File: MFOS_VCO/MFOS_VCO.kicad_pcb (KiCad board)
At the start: 4 copper layers, 100 x 70 mm, 106 parts, among them J12 Conn_01x01, J13 Conn_01x01, J14 Conn_01x01, J15 Conn_01x01, J16 Conn_01x01, J17 Conn_01x01, J18 Conn_01x01, J19 Conn_01x01, J21 Conn_01x01, J22 Conn_01x01, J23 Conn_01x01, J25 Conn_01x01, Q1 PN4391, U1 OP275, U2 TL072, U3 SSM2212, U4 TL074, U5 LM13700, U6 TL072, U7 TL071

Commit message: Laying out
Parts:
- removed J13, J14, J22: Conn_01x01, Connector_Pin:Pin_D1.0mm_L10.0mm_LooseFit
- removed R2, R3, R39: 100k, Resistor_THT:R_Axial_DIN0207_L6.3mm_D2.5mm_P7.62mm_Horizontal
- added J1: Conn_02x05_Odd_Even, Connector_IDC:IDC-Header_2x05_P2.54mm_Vertical, F.Cu at (107.0, 99.5)
- added J24: Conn_01x03, Connector_PinHeader_2.54mm:PinHeader_1x03_P2.54mm_Vertical, F.Cu at (121.7, 68.1)
- added J26: Conn_01x03, Connector_PinHeader_2.54mm:PinHeader_1x03_P2.54mm_Vertical, F.Cu at (121.9, 77.0)
- added J27: Conn_01x03, Connector_PinHeader_2.54mm:PinHeader_1x03_P2.54mm_Vertical, F.Cu at (78.2, 85.9)
- C10, C7: footprint Capacitor_THT:C_Radial_D4.0mm_H5.0mm_P1.50mm -> Capacitor_THT:CP_Radial_D4.0mm_P1.50mm
- J12: value Conn_01x01 -> Conn_01x04; footprint Connector_Pin:Pin_D1.0mm_L10.0mm_LooseFit -> Connector_PinHeader_2.54mm:PinHeader_1x04_P2.54mm_Vertical
- J15: footprint Connector_Pin:Pin_D1.0mm_L10.0mm_LooseFit -> Connector_Pin:Pin_D0.9mm_L10.0mm_W2.4mm_FlatFork
- R11, R16, R5, R59, R60, R64, R7: footprint Resistor_THT:R_Axial_DIN0207_L6.3mm_D2.5mm_P7.62mm_Horizontal -> Potentiometer_THT:Potentiometer_Bourns_3339P_Vertical
- moved U5 296.5 mm to (210.5, 85.9)
- moved R24 224.9 mm to (118.9, 99.8), turned to 90 degrees
- moved C3 224.9 mm to (121.9, 116.1)
- moved D1 219.5 mm to (125.2, 92.5), turned to -90 degrees
- moved U1 216.8 mm to (111.0, 109.2)
- moved R71 215.4 mm to (132.3, 76.7), turned to 180 degrees
- moved C19 215.2 mm to (121.7, 87.6), turned to 90 degrees
- moved R17 211.5 mm to (115.6, 103.6)
- moved R9 211.2 mm to (128.0, 92.5), turned to -90 degrees
- moved R11 210.8 mm to (127.5, 110.2), turned to 90 degrees
- moved R56 203.6 mm to (132.3, 67.6), turned to 180 degrees
- moved R18 199.3 mm to (117.1, 70.4), turned to 180 degrees
- moved R65 196.6 mm to (124.7, 82.8)
- moved R57 194.5 mm to (124.7, 73.7)
- moved U2 192.8 mm to (83.6, 106.2)
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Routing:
- net +12V: track 0.00 -> 313.1 mm, vias 0 -> 5
- net -12V: track 0.00 -> 287.1 mm, vias 0 -> 1
- net Net-(C19-Pad1): track 0.00 -> 84.1 mm, vias 0 -> 2
- net Net-(C3-Pad1): track 0.00 -> 42.1 mm, vias 0 -> 1
- net Net-(C19-Pad2): track 0.00 -> 41.9 mm, vias 0 -> 1
- net Net-(D1-Pad2): track 0.00 -> 25.5 mm, vias 0 -> 1
- net Net-(C3-Pad2): track 0.00 -> 18.0 mm
- net Net-(R17-Pad1): track 0.00 -> 15.3 mm, vias 0 -> 1
- net Net-(R11-Pad1): track 0.00 -> 14.0 mm
- net Net-(R16-Pad3): track 0.00 -> 9.99 mm
- net CV1: track 0.00 -> 3.36 mm
- net /R3P1: track 0.00 -> 3.26 mm
- net CV4: track 0.00 -> 3.26 mm
- net CV2: track 0.00 -> 3.26 mm
- net /R3P3: track 0.00 -> 3.25 mm
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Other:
- rule pad_to_mask_clearance: 3.15 -> 0.0889
- board text added: "+12V"
- board text added: "-12V"
- board text added: "GND"

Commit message: Laid out last part of sheet 1
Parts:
- removed J15: Conn_01x01, Connector_Pin:Pin_D0.9mm_L10.0mm_W2.4mm_FlatFork
- removed J17: Conn_01x01, Connector_Pin:Pin_D1.0mm_L10.0mm_LooseFit
- added J13: Conn_01x02, Connector_PinHeader_2.54mm:PinHeader_1x02_P2.54mm_Vertical, F.Cu at (113.8, 120.1)
- moved C6 254.5 mm to (146.4, 97.8), turned to 180 degrees
- moved C17 244.9 mm to (142.5, 113.5), turned to 90 degrees
- moved D8 239.7 mm to (131.6, 118.6)
- moved R50 232.3 mm to (131.6, 121.4)
- moved R70 228.2 mm to (131.6, 124.7)
- moved R69 226.8 mm to (145.3, 111.3), turned to 90 degrees
- moved R42 219.4 mm to (131.8, 114.3)
- moved R46 211.6 mm to (142.5, 92.5), turned to 180 degrees
- moved C18 209.3 mm to (142.5, 108.9), turned to 90 degrees
- moved C8 204.8 mm to (132.1, 90.2), turned to -90 degrees
- moved R66 203.4 mm to (120.4, 124.7)
- moved R34 194.0 mm to (120.4, 121.7)
- moved Q1 192.6 mm to (128.3, 118.6), turned to 90 degrees
- moved R47 187.9 mm to (142.5, 89.4), turned to 180 degrees
- moved R31 183.6 mm to (114.6, 123.7), turned to 180 degrees
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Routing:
- net LIN: track 2.90 -> 9.84 mm
- net SYNC: track 0.00 -> 2.96 mm
- net Net-(C5-Pad2): track 0.00 -> 2.73 mm
- net GND: track 0.00 -> 2.39 mm, vias 0 -> 1
- net -12V: track 287.1 -> 288.2 mm
- net Net-(D1-Pad2): track 25.5 -> 25.2 mm, vias 1 -> 3

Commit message: All done
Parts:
- removed J16, J18, J19, J21, J23, J25: Conn_01x01, Connector_Pin:Pin_D1.0mm_L10.0mm_LooseFit
- added G***: LOGO, LOGO, F.Cu at (194.6, 119.9)
- added J14: Conn_01x02, Connector_PinHeader_2.54mm:PinHeader_1x02_P2.54mm_Vertical, F.Cu at (194.6, 73.4)
- added J15: Conn_01x04, Connector_PinHeader_2.54mm:PinHeader_1x04_P2.54mm_Vertical, F.Cu at (191.0, 105.2)
- added kibuzzard-65B0951C: G***, kibuzzard-65B0951C, F.Cu at (110.2, 62.2)
- added kibuzzard-65B09543: G***, kibuzzard-65B09543, F.Cu at (190.5, 119.6)
- C12: footprint Capacitor_THT:CP_Radial_D8.0mm_P3.50mm -> Capacitor_THT:CP_Radial_D5.0mm_P2.00mm
- C13: footprint Capacitor_THT:CP_Radial_D8.0mm_P3.50mm -> Capacitor_THT:CP_Radial_D5.0mm_P2.50mm
- moved R36 292.6 mm to (188.0, 99.3)
- moved U7 281.1 mm to (177.0, 86.6)
- moved R64 280.8 mm to (176.3, 111.3)
- moved R67 279.5 mm to (173.7, 93.2), turned to 180 degrees
- moved R60 278.4 mm to (184.6, 111.2)
- moved D4 278.3 mm to (171.4, 75.2), turned to 180 degrees
- moved R40 271.0 mm to (166.1, 90.2)
- moved R49 269.9 mm to (186.7, 124.2), turned to 90 degrees
- moved R48 269.1 mm to (163.8, 116.6), turned to -90 degrees
- moved R41 267.8 mm to (195.6, 96.0), turned to 180 degrees
- moved R53 264.3 mm to (180.6, 124.2), turned to 90 degrees
- moved U4 262.9 mm to (153.4, 87.1)
- moved R29 261.6 mm to (167.9, 100.8)
- moved R35 261.1 mm to (177.0, 83.3)
- moved U6 259.9 mm to (177.0, 68.8)
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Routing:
- net +12V: track 313.1 -> 481.0 mm, vias 5 -> 11
- net -12V: track 288.2 -> 395.1 mm, vias 1 -> 2
- net Net-(C6-Pad1): track 0.00 -> 67.5 mm, vias 0 -> 4
- net Net-(D3-Pad2): track 0.00 -> 62.5 mm
- net TRI: track 0.00 -> 61.3 mm, vias 0 -> 3
- net Net-(R14-Pad2): track 0.00 -> 47.2 mm, vias 0 -> 3
- net PWM: track 0.00 -> 46.8 mm, vias 0 -> 1
- net RMP: track 0.00 -> 45.3 mm
- net Net-(R34-Pad2): track 0.00 -> 44.4 mm, vias 0 -> 3
- net Net-(C12-Pad2): track 0.00 -> 41.9 mm, vias 0 -> 4
- net RAW: track 0.00 -> 40.5 mm, vias 0 -> 2
- net Net-(C2-Pad1): track 0.00 -> 40.0 mm, vias 0 -> 1
- net Net-(C14-Pad1): track 0.00 -> 33.7 mm, vias 0 -> 3
- net Net-(R13-Pad2): track 0.00 -> 32.6 mm, vias 0 -> 1
- net Net-(R45-Pad2): track 0.00 -> 31.9 mm, vias 0 -> 3
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- added copper zone on F.Cu, net (none)

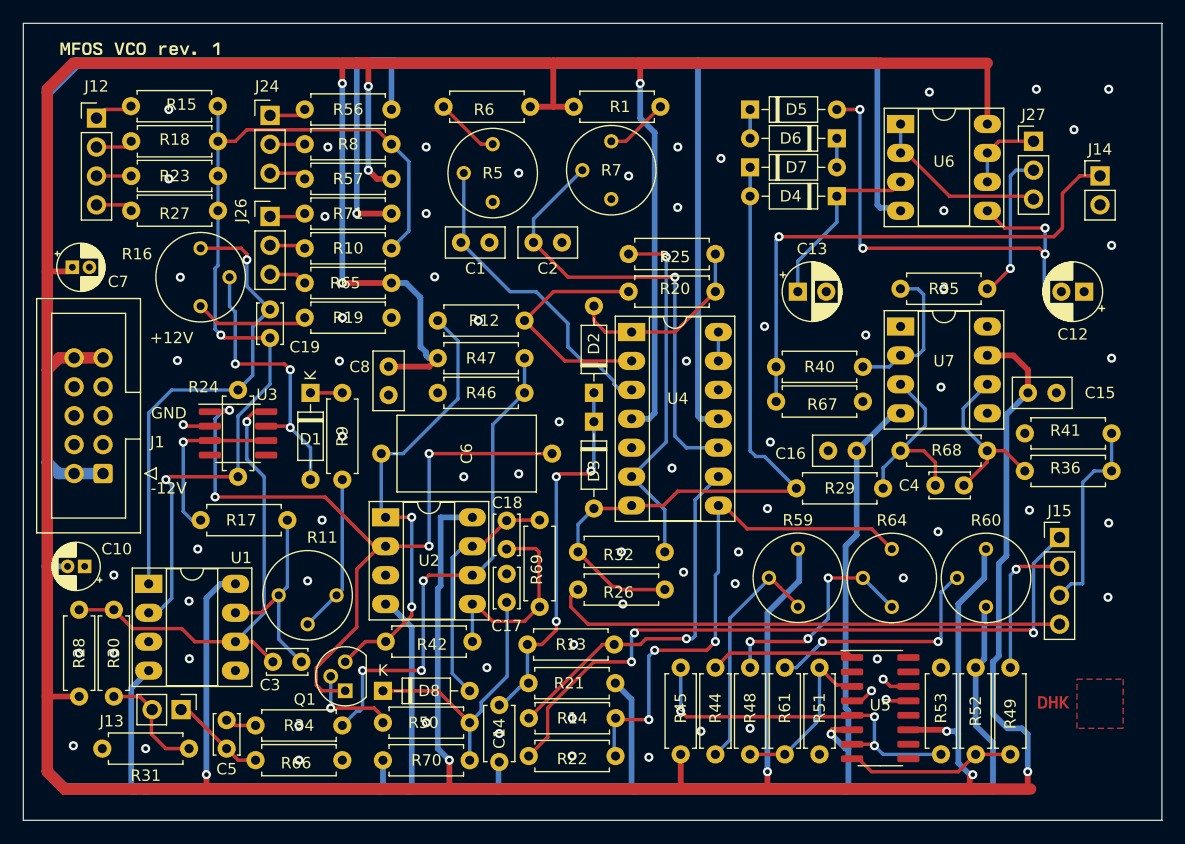
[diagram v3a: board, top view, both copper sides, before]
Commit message: Fixed PN4391 bug. Made some layout changes. Fitted molex connectors instead of pin connectors
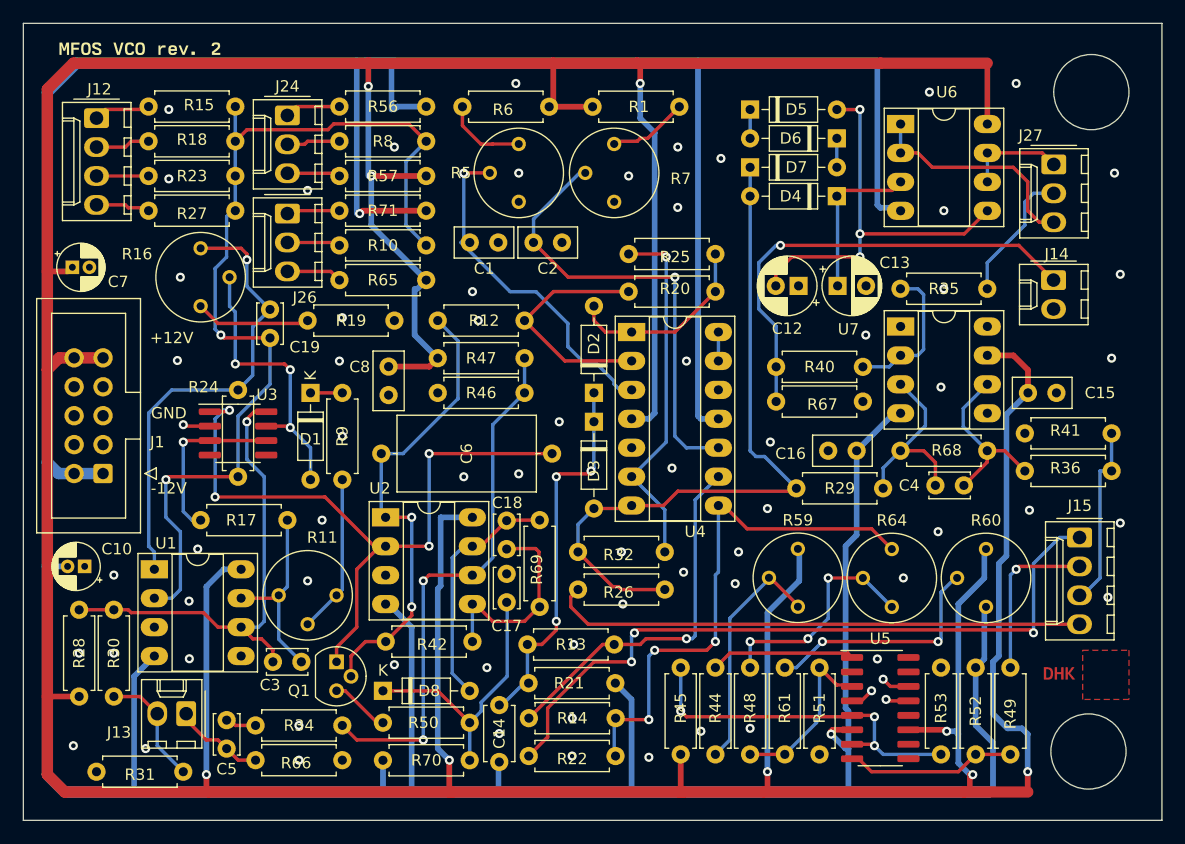
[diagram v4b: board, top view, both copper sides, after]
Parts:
- removed kibuzzard-65B0951C: G***, kibuzzard-65B0951C
- added kibuzzard-660EFCED: G***, kibuzzard-660EFCED, F.Cu at (110.2, 62.2)
- J12, J15: footprint Connector_PinHeader_2.54mm:PinHeader_1x04_P2.54mm_Vertical -> Connector_Molex:Molex_KK-254_AE-6410-04A_1x04_P2.54mm_Vertical
- J13, J14: footprint Connector_PinHeader_2.54mm:PinHeader_1x02_P2.54mm_Vertical -> Connector_Molex:Molex_KK-254_AE-6410-02A_1x02_P2.54mm_Vertical
- J24, J26, J27: footprint Connector_PinHeader_2.54mm:PinHeader_1x03_P2.54mm_Vertical -> Connector_Molex:Molex_KK-254_AE-6410-03A_1x03_P2.54mm_Vertical
- moved C12 25.1 mm to (168.1, 83.1)
- moved J14 10.0 mm to (190.5, 82.5), turned to -90 degrees
- moved C13 3.53 mm to (171.5, 83.1)
- moved R10 3.06 mm to (127.8, 79.5)
- moved R65 3.06 mm to (127.8, 82.5)
- moved R71 3.06 mm to (135.4, 76.5)
- moved R56 3.06 mm to (135.4, 67.3)
- moved R57 3.06 mm to (127.8, 73.4)
- moved R8 3.06 mm to (127.8, 70.4)
- moved J27 2.70 mm to (190.5, 72.4), turned to -90 degrees
- moved Q1 2.65 mm to (127.5, 116.1), turned to -90 degrees
- moved G*** 2.59 mm to (195.1, 117.3)
- moved kibuzzard-65B09543 2.59 mm to (191.0, 117.1)
- moved R5 2.29 mm to (143.5, 75.7)
- moved R31 2.09 mm to (114.0, 125.7)
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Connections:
- Q1 pad 2: Net-(Q1-Pad2) -> RAW
- Q1 pad 3: RAW -> Net-(Q1-Pad3)
- R50 pad 1: Net-(Q1-Pad2) -> Net-(Q1-Pad3)
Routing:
- net +12V: track 481.0 -> 470.9 mm, vias 11 -> 9
- net Net-(Q1-Pad2): track 8.20 -> 0.00 mm, vias 1 -> 0
- net -12V: track 395.1 -> 402.2 mm
- net PWM: track 46.8 -> 40.6 mm
- net Net-(C12-Pad2): track 41.9 -> 36.1 mm, vias 4 -> 3
- net Net-(C6-Pad1): track 67.5 -> 62.0 mm
- net Net-(Q1-Pad3): track 0.00 -> 5.24 mm
- net /Sheet 2/R39P3: track 15.9 -> 20.0 mm
- net Net-(R34-Pad2): track 44.4 -> 47.2 mm, vias 3 -> 2
- net Net-(C19-Pad1): track 84.1 -> 86.7 mm
- net Net-(C13-Pad1): track 16.2 -> 13.8 mm
- net Net-(C1-Pad1): track 27.9 -> 30.2 mm, vias 0 -> 1
- net /R3P3: track 3.25 -> 5.11 mm
- net /R2P3: track 3.10 -> 4.89 mm
- net /Sheet 2/R39P1: track 7.02 -> 8.79 mm
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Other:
- outline, holes or cut-outs redrawn
- rule pad_to_mask_clearance: 0.0889 -> 0

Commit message: Some bugfixes
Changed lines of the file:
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@@
     (pad_to_mask_clearance 0)
     (pcbplotparams
-      (layerselection 0x00010fc_ffffffff)
+      (layerselection 0x00010f0_ffffffff)
       (disableapertmacros false)
-      (usegerberextensions false)
+      (usegerberextensions true)
       (usegerberattributes true)
       (usegerberadvancedattributes true)
@@
     (fp_line (start -1.27 2.88) (end 6.35 2.88) (layer "F.Fab") (width 0.1))
     (fp_line (start 6.35 -2.92) (end -1.27 -2.92) (layer "F.Fab") (width 0.1))
-    (pad "1" thru_hole roundrect (at 0 0 270) (size 1.74 2.19) (drill 1.19) (layers *.Cu *.Mask) (roundrect_rratio 0.143678)
+    (pad "1" thru_hole roundrect (at 0 0 270) (size 1.74 2.19) (drill 1.19) (layers *.Cu *.Mask) (roundrect_rratio 0.1436781609)
       (net 55 "/Sheet 2/R39P1") (pinfunction "Pin_1") (pintype "passive"))
     (pad "2" thru_hole oval (at 2.54 0 270) (size 1.74 2.19) (drill 1.19) (layers *.Cu *.Mask)
@@
     (fp_line (start -1.27 2.88) (end 3.81 2.88) (layer "F.Fab") (width 0.1))
     (fp_line (start 3.81 -2.92) (end -1.27 -2.92) (layer "F.Fab") (width 0.1))
-    (pad "1" thru_hole roundrect (at 0 0 180) (size 1.74 2.19) (drill 1.19) (layers *.Cu *.Mask) (roundrect_rratio 0.143678)
+    (pad "1" thru_hole roundrect (at 0 0 180) (size 1.74 2.19) (drill 1.19) (layers *.Cu *.Mask) (roundrect_rratio 0.1436781609)
       (net 8 "SYNC") (pinfunction "Pin_1") (pintype "passive"))
     (pad "2" thru_hole oval (at 2.54 0 180) (size 1.74 2.19) (drill 1.19) (layers *.Cu *.Mask)
@@
     (fp_line (start -1.27 2.88) (end 6.35 2.88) (layer "F.Fab") (width 0.1))
     (fp_line (start -0.562893 0) (end -1.27 0.5) (layer "F.Fab") (width 0.1))
-    (pad "1" thru_hole roundrect (at 0 0 270) (size 1.74 2.19) (drill 1.19) (layers *.Cu *.Mask) (roundrect_rratio 0.143678)
+    (pad "1" thru_hole roundrect (at 0 0 270) (size 1.74 2.19) (drill 1.19) (layers *.Cu *.Mask) (roundrect_rratio 0.1436781609)
       (net 40 "/R2P1") (pinfunction "Pin_1") (pintype "passive"))
     (pad "2" thru_hole oval (at 2.54 0 270) (size 1.74 2.19) (drill 1.19) (layers *.Cu *.Mask)
@@
     (fp_line (start 8.89 2.88) (end 8.89 -2.92) (layer "F.Fab") (width 0.1))
     (fp_line (start -0.562893 0) (end -1.27 0.5) (layer "F.Fab") (width 0.1))
-    (pad "1" thru_hole roundrect (at 0 0 270) (size 1.74 2.19) (drill 1.19) (layers *.Cu *.Mask) (roundrect_rratio 0.143678)
+    (pad "1" thru_hole roundrect (at 0 0 270) (size 1.74 2.19) (drill 1.19) (layers *.Cu *.Mask) (roundrect_rratio 0.1436781609)
       (net 33 "TRI") (pinfunction "Pin_1") (pintype "passive"))
     (pad "2" thru_hole oval (at 2.54 0 270) (size 1.74 2.19) (drill 1.19) (layers *.Cu *.Mask)
@@
     (fp_line (start -1.27 -0.5) (end -0.562893 0) (layer "F.Fab") (width 0.1))
     (fp_line (start 8.89 2.88) (end 8.89 -2.92) (layer "F.Fab") (width 0.1))
-    (pad "1" thru_hole roundrect (at 0 0 270) (size 1.74 2.19) (drill 1.19) (layers *.Cu *.Mask) (roundrect_rratio 0.143678)
+    (pad "1" thru_hole roundrect (at 0 0 270) (size 1.74 2.19) (drill 1.19) (layers *.Cu *.Mask) (roundrect_rratio 0.1436781609)
       (net 28 "CV1") (pinfunction "Pin_1") (pintype "passive"))
     (pad "2" thru_hole oval (at 2.54 0 270) (size 1.74 2.19) (drill 1.19) (layers *.Cu *.Mask)
@@
     (fp_line (start 3.81 -2.92) (end -1.27 -2.92) (layer "F.Fab") (width 0.1))
     (fp_line (start -1.27 -2.92) (end -1.27 2.88) (layer "F.Fab") (width 0.1))
-    (pad "1" thru_hole roundrect (at 0 0 270) (size 1.74 2.19) (drill 1.19) (layers *.Cu *.Mask) (roundrect_rratio 0.143678)
+    (pad "1" thru_hole roundrect (at 0 0 270) (size 1.74 2.19) (drill 1.19) (layers *.Cu *.Mask) (roundrect_rratio 0.1436781609)
       (net 32 "PWM") (pinfunction "Pin_1") (pintype "passive"))
     (pad "2" thru_hole oval (at 2.54 0 270) (size 1.74 2.19) (drill 1.19) (layers *.Cu *.Mask)
@@
     (fp_line (start -1.27 -2.92) (end -1.27 2.88) (layer "F.Fab") (width 0.1))
     (fp_line (start 6.35 -2.92) (end -1.27 -2.92) (layer "F.Fab") (width 0.1))
-    (pad "1" thru_hole roundrect (at 0 0 270) (size 1.74 2.19) (drill 1.19) (layers *.Cu *.Mask) (roundrect_rratio 0.143678)
+    (pad "1" thru_hole roundrect (at 0 0 270) (size 1.74 2.19) (drill 1.19) (layers *.Cu *.Mask) (roundrect_rratio 0.1436781609)
       (net 42 "/R3P1") (pinfunction "Pin_1") (pintype "passive"))
     (pad "2" thru_hole oval (at 2.54 0 270) (size 1.74 2.19) (drill 1.19) (layers *.Cu *.Mask)
